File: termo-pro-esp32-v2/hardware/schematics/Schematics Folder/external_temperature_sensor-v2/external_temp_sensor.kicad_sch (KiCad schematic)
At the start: 1 part

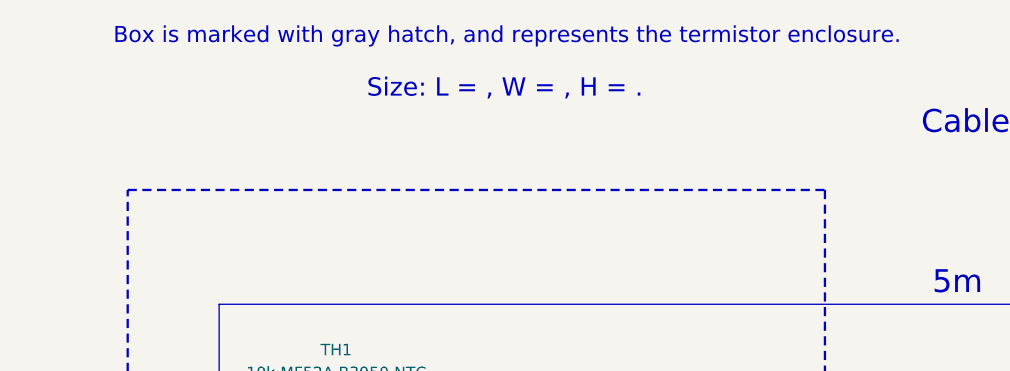
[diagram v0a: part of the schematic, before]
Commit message: Hardware part of the project is finished.
-DHT11 placement on thermostat unit fixed, pins trace redone.
-USB-C port on thermostat unit placed closer to edge by 4mm.
-Capacitors values recalculated and updated to closest common values, resistors values too.
-Starting unit pcb redone traces as relay and caps have been moved to the back plate.

-Starting & thermostat units PCB are done, inspected.
-Ready for fabrication.
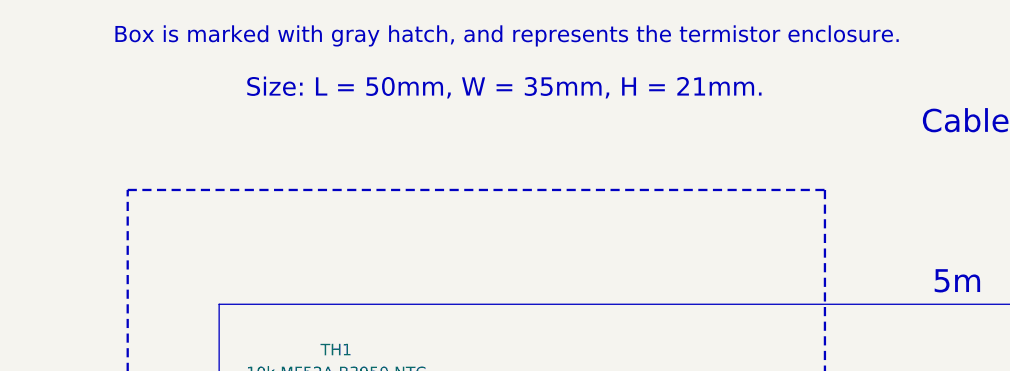
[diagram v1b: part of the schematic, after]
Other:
- note added: "Size: L = 50mm, W = 35mm, H = 21mm."
- note removed: "Size: L = , W = , H = ."
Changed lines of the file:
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@@
 		)
 	)
-	(text "Size: L = , W = , H = . "
+	(text "Size: L = 50mm, W = 35mm, H = 21mm. "
 		(exclude_from_sim no)
 		(at 69.85 73.914 0)
